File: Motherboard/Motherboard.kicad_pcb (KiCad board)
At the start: 2 copper layers, 100 x 100 mm, 334 parts, among them J1 Signal_socket, J2 ATX_power, J3 RPi_server, J4 Power_socket, J5 Test_~PS_ON~, Q1 2SA1015, SW1 Reset, U1 LM358, U2 ATtiny13A-PU

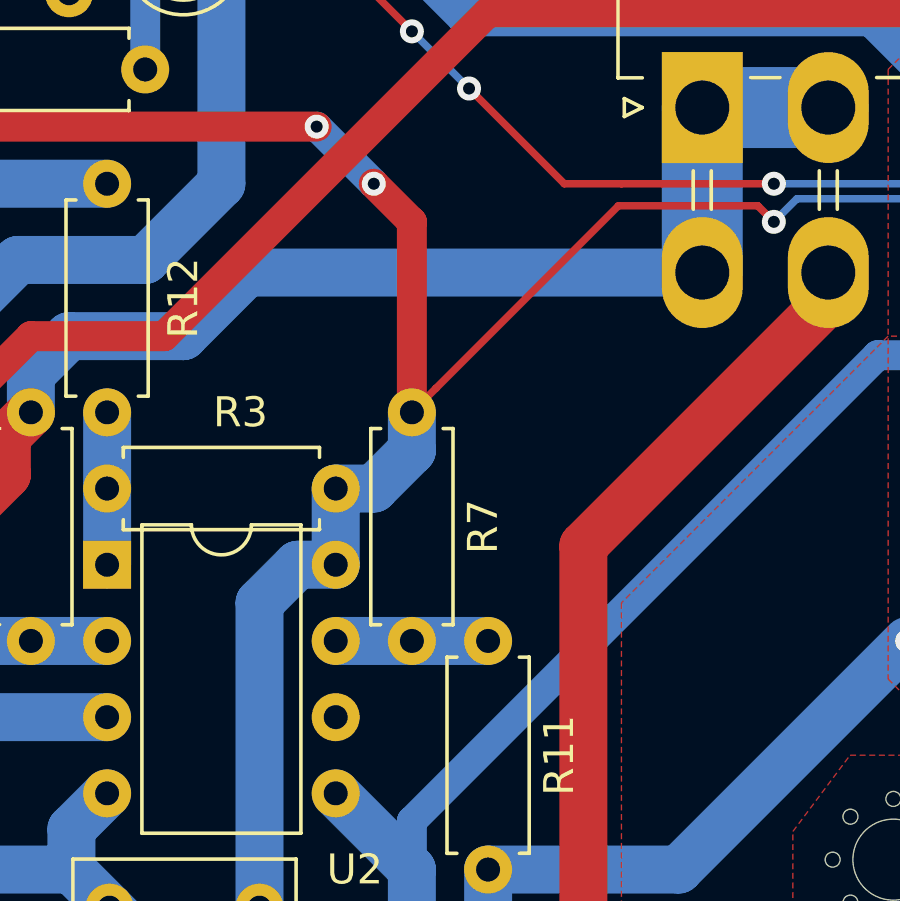
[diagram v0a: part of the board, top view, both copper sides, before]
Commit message: Motherboard: Also monitor the PS_OK line
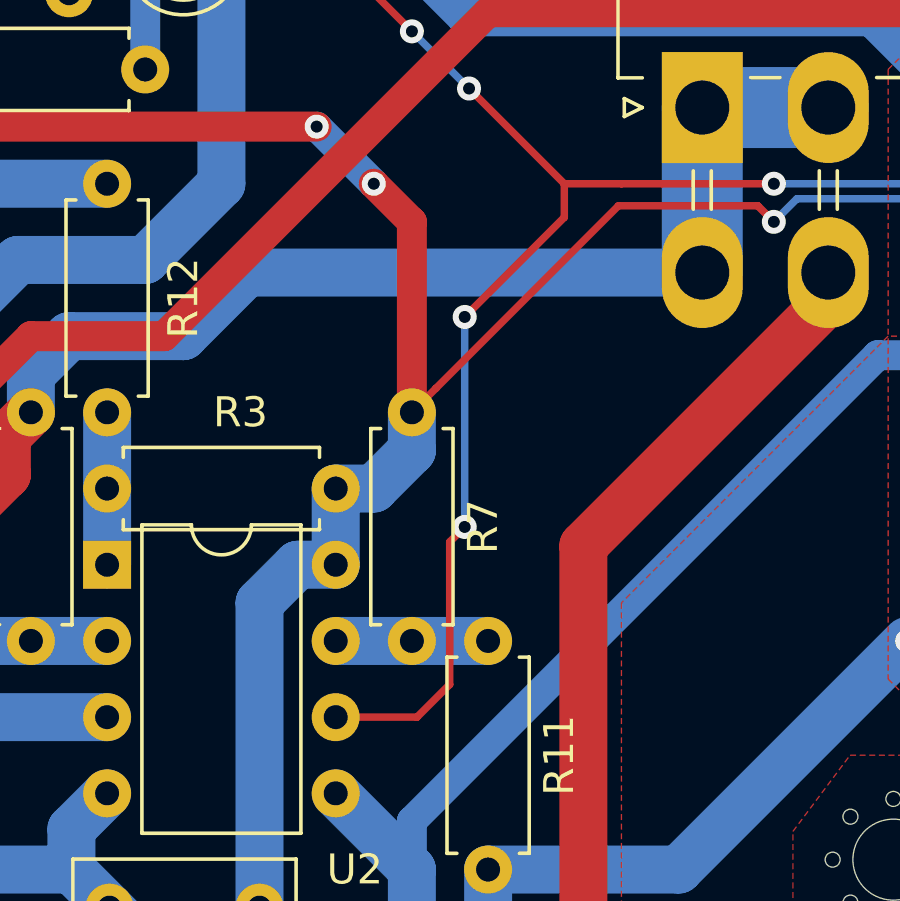
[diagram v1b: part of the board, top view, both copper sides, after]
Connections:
- J2 pad 10: (no net) -> Net-(J2-Pad10)
- J2 pad 11: (no net) -> Net-(J2-Pad11)
- J2 pad 20: (no net) -> Net-(J2-Pad20)
- J3 pad 1: (no net) -> Net-(J3-Pad1)
- J3 pad 11: (no net) -> Net-(J3-Pad11)
- J3 pad 12: (no net) -> Net-(J3-Pad12)
- J3 pad 13: (no net) -> Net-(J3-Pad13)
- J3 pad 15: (no net) -> Net-(J3-Pad15)
- J3 pad 16: (no net) -> Net-(J3-Pad16)
- J3 pad 17: (no net) -> Net-(J3-Pad17)
- J3 pad 18: (no net) -> Net-(J3-Pad18)
- J3 pad 19: (no net) -> Net-(J3-Pad19)
- J3 pad 21: (no net) -> Net-(J3-Pad21)
- J3 pad 22: (no net) -> Net-(J3-Pad22)
- J3 pad 23: (no net) -> Net-(J3-Pad23)
- J3 pad 24: (no net) -> Net-(J3-Pad24)
- J3 pad 26: (no net) -> Net-(J3-Pad26)
- J3 pad 27: (no net) -> Net-(J3-Pad27)
- J3 pad 28: (no net) -> Net-(J3-Pad28)
- J3 pad 29: (no net) -> Net-(J3-Pad29)
- J3 pad 31: (no net) -> Net-(J3-Pad31)
- J3 pad 32: (no net) -> Net-(J3-Pad32)
- J3 pad 33: (no net) -> Net-(J3-Pad33)
- J3 pad 35: (no net) -> Net-(J3-Pad35)
- J3 pad 36: (no net) -> Net-(J3-Pad36)
- J3 pad 37: (no net) -> Net-(J3-Pad37)
- J3 pad 38: (no net) -> Net-(J3-Pad38)
- J3 pad 40: (no net) -> Net-(J3-Pad40)
- J3 pad 7: (no net) -> Net-(J3-Pad7)
- U2 pad 6: (no net) -> /PWR_OK
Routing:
- net /PWR_OK: track 57.6 -> 80.2 mm, vias 3 -> 5
